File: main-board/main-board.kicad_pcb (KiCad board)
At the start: 2 copper layers, 210 x 130 mm, 199 parts, among them J1 PWR_SELECT, J10 Conn_02x05_Odd_Even, J11 Conn_02x05_Odd_Even, J12 Conn_02x05_Odd_Even, J13 Conn_02x05_Odd_Even, J14 Conn_02x05_Odd_Even, J15 Conn_02x05_Odd_Even, J16 COMM_3, J17 Modular board connector, J18 PWR_EXT_1, J19 PWR_EXT_2, J2 COMM1, J20 COMM_4, J21 COMM_OUT, J3 ICSP, J5 COMM_2, J7 Conn_02x05_Odd_Even, J8 Conn_02x05_Odd_Even, J9 Conn_02x05_Odd_Even, SW1 RESET, SW10 SW_Push, SW11 SW_Push, SW12 SW_SP3T_x08, SW13 SW_Push, SW14 SW_Push, SW15 SW_Push, SW16 SW_Push, SW17 SW_Push, SW18 SW_Push, SW19 SW_Push, SW2 BTN_LEVEL, SW20 SW_Push, SW21 SW_SP3T_x08, SW22 SW_Push, SW23 SW_Push, SW24 SW_Push, SW25 SW_Push, SW26 SW_Push, SW27 SW_Push, SW28 SW_Push, SW29 SW_Push, SW3 LED_GND, SW30 SW_SP3T_x08, SW31 SW_Push, SW32 SW_Push, SW33 SW_Push, SW34 SW_Push, SW35 SW_Push, SW36 SW_Push, SW37 SW_Push, SW38 SW_Push, SW39 SW_SP3T_x08, SW4 SW_Push, SW41 PWR_EN, SW5 SW_Push, SW6 SW_Push, SW7 SW_Push, SW8 SW_Push, SW9 SW_Push, U1 LM2576HVS-5, U2 AP1117-33, U3 AP1117-18, U4 FT232RL

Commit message: Changed ICP header to IDC connector
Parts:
- J3: footprint Connector_PinHeader_2.54mm:PinHeader_2x05_P2.54mm_Vertical -> Connector_IDC:IDC-Header_2x05_P2.54mm_Vertical
- TP_GND3: value VBUS -> GND
- TP_VBUS2: value GND -> VBUS
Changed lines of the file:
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@@
     (add_net "Net-(J17-Pad30)")
     (add_net "Net-(J17-Pad32)")
+    (add_net "Net-(J17-Pad34)")
+    (add_net "Net-(J17-Pad56)")
     (add_net "Net-(J17-Pad58)")
     (add_net "Net-(J17-Pad60)")
+    (add_net "Net-(J17-Pad75)")
     (add_net "Net-(J21-Pad2)")
     (add_net "Net-(J21-Pad3)")
@@
     (add_net "Net-(R71-Pad2)")
     (add_net "Net-(R72-Pad2)")
+    (add_net "Net-(SW41-Pad3)")
+    (add_net "Net-(U4-Pad10)")
+    (add_net "Net-(U4-Pad12)")
+    (add_net "Net-(U4-Pad13)")
+    (add_net "Net-(U4-Pad14)")
     (add_net "Net-(U4-Pad15)")
     (add_net "Net-(U4-Pad16)")
+    (add_net "Net-(U4-Pad19)")
+    (add_net "Net-(U4-Pad27)")
+    (add_net "Net-(U4-Pad28)")
+    (add_net "Net-(U4-Pad4)")
+    (add_net "Net-(U4-Pad6)")
+    (add_net "Net-(U4-Pad9)")
     (add_net VBUS)
   )
@@
     (uvia_drill 0.1)
   )
+  (module Connector_IDC:IDC-Header_2x05_P2.54mm_Vertical locked (layer F.Cu)
+    (at 66 140.8 270)
+    (descr "Through hole straight IDC box header, 2x05, 2.54mm pitch, double rows")
+    (tags "Through hole IDC box header THT 2x05 2.54mm double row")
+    (fp_text reference J3 (at 1.27 -6.604 90) (layer F.SilkS)
+      (effects (font (size 1 1) (thickness 0.15)))
+    )
+    (fp_text value ICSP (at 1.27 16.764 90) (layer F.Fab)
+      (effects (font (size 1 1) (thickness 0.15)))
+    )
+    (fp_line (start -3.655 -5.6) (end -1.115 -5.6) (layer F.SilkS) (width 0.12))
+    (fp_line (start -3.655 -5.6) (end -3.655 -3.06) (layer F.SilkS) (width 0.12))
+    (fp_line (start -3.405 -5.35) (end 5.945 -5.35) (layer F.SilkS) (width 0.12))
+    (fp_line (start -3.405 15.51) (end -3.405 -5.35) (layer F.SilkS) (width 0.12))
+    (fp_line (start 5.945 15.51) (end -3.405 15.51) (layer F.SilkS) (width 0.12))
+    (fp_line (start 5.945 -5.35) (end 5.945 15.51) (layer F.SilkS) (width 0.12))
+    (fp_line (start -3.41 -5.35) (end 5.95 -5.35) (layer F.CrtYd) (width 0.05))
+    (fp_line (start -3.41 15.51) (end -3.41 -5.35) (layer F.CrtYd) (width 0.05))
+    (fp_line (start 5.95 15.51) (end -3.41 15.51) (layer F.CrtYd) (width 0.05))
+    (fp_line (start 5.95 -5.35) (end 5.95 15.51) (layer F.CrtYd) (width 0.05))
+    (fp_line (start -3.155 15.26) (end -2.605 14.7) (layer F.Fab) (width 0.1))
+    (fp_line (start -3.155 -5.1) (end -2.605 -4.56) (layer F.Fab) (width 0.1))
+    (fp_line (start 5.695 15.26) (end 5.145 14.7) (layer F.Fab) (width 0.1))
+    (fp_line (start 5.695 -5.1) (end 5.145 -4.56) (layer F.Fab) (width 0.1))
+    (fp_line (start 5.145 14.7) (end -2.605 14.7) (layer F.Fab) (width 0.1))
+    (fp_line (start 5.695 15.26) (end -3.155 15.26) (layer F.Fab) (width 0.1))
+    (fp_line (start 5.145 -4.56) (end -2.605 -4.56) (layer F.Fab) (width 0.1))
+    (fp_line (start 5.695 -5.1) (end -3.155 -5.1) (layer F.Fab) (width 0.1))
+    (fp_line (start -2.605 7.33) (end -3.155 7.33) (layer F.Fab) (width 0.1))
+    (fp_line (start -2.605 2.83) (end -3.155 2.83) (layer F.Fab) (width 0.1))
+    (fp_line (start -2.605 7.33) (end -2.605 14.7) (layer F.Fab) (width 0.1))
+    (fp_line (start -2.605 -4.56) (end -2.605 2.83) (layer F.Fab) (width 0.1))
+    (fp_line (start -3.155 -5.1) (end -3.155 15.26) (layer F.Fab) (width 0.1))
+    (fp_line (start 5.145 -4.56) (end 5.145 14.7) (layer F.Fab) (width 0.1))
+    (fp_line (start 5.695 -5.1) (end 5.695 15.26) (layer F.Fab) (width 0.1))
+    (fp_text user %R (at 1.27 5.08 90) (layer F.Fab)
+      (effects (font (size 1 1) (thickness 0.15)))
+    )
+    (pad 10 thru_hole oval (at 2.54 10.16 270) (size 1.7272 1.7272) (drill 1.016) (layers *.Cu *.Mask)
+      (net 38 ICSP10))
+    (pad 9 thru_hole oval (at 0 10.16 270) (size 1.7272 1.7272) (drill 1.016) (layers *.Cu *.Mask)
+      (net 39 ICSP9))
+    (pad 8 thru_hole oval (at 2.54 7.62 270) (size 1.7272 1.7272) (drill 1.016) (layers *.Cu *.Mask)
+      (net 40 ICSP8))
+    (pad 7 thru_hole oval (at 0 7.62 270) (size 1.7272 1.7272) (drill 1.016) (layers *.Cu *.Mask)
+      (net 41 ICSP7))
+    (pad 6 thru_hole oval (at 2.54 5.08 270) (size 1.7272 1.7272) (drill 1.016) (layers *.Cu *.Mask)
+      (net 42 ICSP6))
+    (pad 5 thru_hole oval (at 0 5.08 270) (size 1.7272 1.7272) (drill 1.016) (layers *.Cu *.Mask)
+      (net 43 ICSP5))
+    (pad 4 thru_hole oval (at 2.54 2.54 270) (size 1.7272 1.7272) (drill 1.016) (layers *.Cu *.Mask)
+      (net 44 ICSP4))
+    (pad 3 thru_hole oval (at 0 2.54 270) (size 1.7272 1.7272) (drill 1.016) (layers *.Cu *.Mask)
+      (net 45 ICSP3))
+    (pad 2 thru_hole oval (at 2.54 0 270) (size 1.7272 1.7272) (drill 1.016) (layers *.Cu *.Mask)
+      (net 46 ICSP2))
+    (pad 1 thru_hole rect (at 0 0 270) (size 1.7272 1.7272) (drill 1.016) (layers *.Cu *.Mask)
+      (net 125 ICSP1))
+    (model ${KISYS3DMOD}/Connector_IDC.3dshapes/IDC-Header_2x05_P2.54mm_Vertical.wrl
+      (at (xyz 0 0 0))
+      (scale (xyz 1 1 1))
+      (rotate (xyz 0 0 0))
+    )
+  )
   (module TestPoint:TestPoint_Plated_Hole_D2.0mm (layer F.Cu)
     (at 162 144.9)
@@
     )
   )
-  (module Connector_PinHeader_2.54mm:PinHeader_2x05_P2.54mm_Vertical locked (layer F.Cu)
-    (at 66 140.8 270)
-    (descr "Through hole straight pin header, 2x05, 2.54mm pitch, double rows")
-    (tags "Through hole pin header THT 2x05 2.54mm double row")
-    (fp_text reference J3 (at 1.27 -2.33 90 unlocked) (layer F.SilkS) hide
-      (effects (font (size 0.7 0.7) (thickness 0.15)))
-    )
-    (fp_text value ICSP (at 1.27 12.49 90) (layer F.Fab)
-      (effects (font (size 1 1) (thickness 0.15)))
-    )
-    (fp_text user %R (at 1.27 5.08) (layer F.Fab) hide
-      (effects (font (size 1 1) (thickness 0.15)))
-    )
-    (fp_line (start 4.35 -1.8) (end -1.8 -1.8) (layer F.CrtYd) (width 0.05))
-    (fp_line (start 4.35 11.95) (end 4.35 -1.8) (layer F.CrtYd) (width 0.05))
-    (fp_line (start -1.8 11.95) (end 4.35 11.95) (layer F.CrtYd) (width 0.05))
-    (fp_line (start -1.8 -1.8) (end -1.8 11.95) (layer F.CrtYd) (width 0.05))
-    (fp_line (start -1.33 -1.33) (end 0 -1.33) (layer F.SilkS) (width 0.12))
-    (fp_line (start -1.33 0) (end -1.33 -1.33) (layer F.SilkS) (width 0.12))
-    (fp_line (start 1.27 -1.33) (end 3.87 -1.33) (layer F.SilkS) (width 0.12))
-    (fp_line (start 1.27 1.27) (end 1.27 -1.33) (layer F.SilkS) (width 0.12))
-    (fp_line (start -1.33 1.27) (end 1.27 1.27) (layer F.SilkS) (width 0.12))
-    (fp_line (start 3.87 -1.33) (end 3.87 11.49) (layer F.SilkS) (width 0.12))
-    (fp_line (start -1.33 1.27) (end -1.33 11.49) (layer F.SilkS) (width 0.12))
-    (fp_line (start -1.33 11.49) (end 3.87 11.49) (layer F.SilkS) (width 0.12))
-    (fp_line (start -1.27 0) (end 0 -1.27) (layer F.Fab) (width 0.1))
-    (fp_line (start -1.27 11.43) (end -1.27 0) (layer F.Fab) (width 0.1))
-    (fp_line (start 3.81 11.43) (end -1.27 11.43) (layer F.Fab) (width 0.1))
-    (fp_line (start 3.81 -1.27) (end 3.81 11.43) (layer F.Fab) (width 0.1))
-    (fp_line (start 0 -1.27) (end 3.81 -1.27) (layer F.Fab) (width 0.1))
-    (pad 10 thru_hole oval (at 2.54 10.16 270) (size 1.7 1.7) (drill 1) (layers *.Cu *.Mask)
-      (net 38 ICSP10))
-    (pad 9 thru_hole oval (at 0 10.16 270) (size 1.7 1.7) (drill 1) (layers *.Cu *.Mask)
-      (net 39 ICSP9))
-    (pad 8 thru_hole oval (at 2.54 7.62 270) (size 1.7 1.7) (drill 1) (layers *.Cu *.Mask)
-      (net 40 ICSP8))
-    (pad 7 thru_hole oval (at 0 7.62 270) (size 1.7 1.7) (drill 1) (layers *.Cu *.Mask)
-      (net 41 ICSP7))
-    (pad 6 thru_hole oval (at 2.54 5.08 270) (size 1.7 1.7) (drill 1) (layers *.Cu *.Mask)
-      (net 42 ICSP6))
-    (pad 5 thru_hole oval (at 0 5.08 270) (size 1.7 1.7) (drill 1) (layers *.Cu *.Mask)
-      (net 43 ICSP5))
-    (pad 4 thru_hole oval (at 2.54 2.54 270) (size 1.7 1.7) (drill 1) (layers *.Cu *.Mask)
-      (net 44 ICSP4))
-    (pad 3 thru_hole oval (at 0 2.54 270) (size 1.7 1.7) (drill 1) (layers *.Cu *.Mask)
-      (net 45 ICSP3))
-    (pad 2 thru_hole oval (at 2.54 0 270) (size 1.7 1.7) (drill 1) (layers *.Cu *.Mask)
-      (net 46 ICSP2))
-    (pad 1 thru_hole rect (at 0 0 270) (size 1.7 1.7) (drill 1) (layers *.Cu *.Mask)
-      (net 125 ICSP1))
-    (model ${KISYS3DMOD}/Connector_PinHeader_2.54mm.3dshapes/PinHeader_2x05_P2.54mm_Vertical.wrl
-      (at (xyz 0 0 0))
-      (scale (xyz 1 1 1))
-      (rotate (xyz 0 0 0))
-    )
-  )
   (module MountingHole:MountingHole_3.2mm_M3_ISO14580_Pad locked (layer F.Cu)
     (at 242 23)
@@
       (effects (font (size 1 1) (thickness 0.15)))
     )
-    (fp_text value VBUS (at 0 2.45) (layer F.Fab)
+    (fp_text value GND (at 0 2.45) (layer F.Fab)
       (effects (font (size 1 1) (thickness 0.15)))
     )
@@
       (effects (font (size 1 1) (thickness 0.15)))
     )
-    (fp_text value GND (at 0 2.45) (layer F.Fab)
+    (fp_text value VBUS (at 0 2.45) (layer F.Fab)
       (effects (font (size 1 1) (thickness 0.15)))
     )

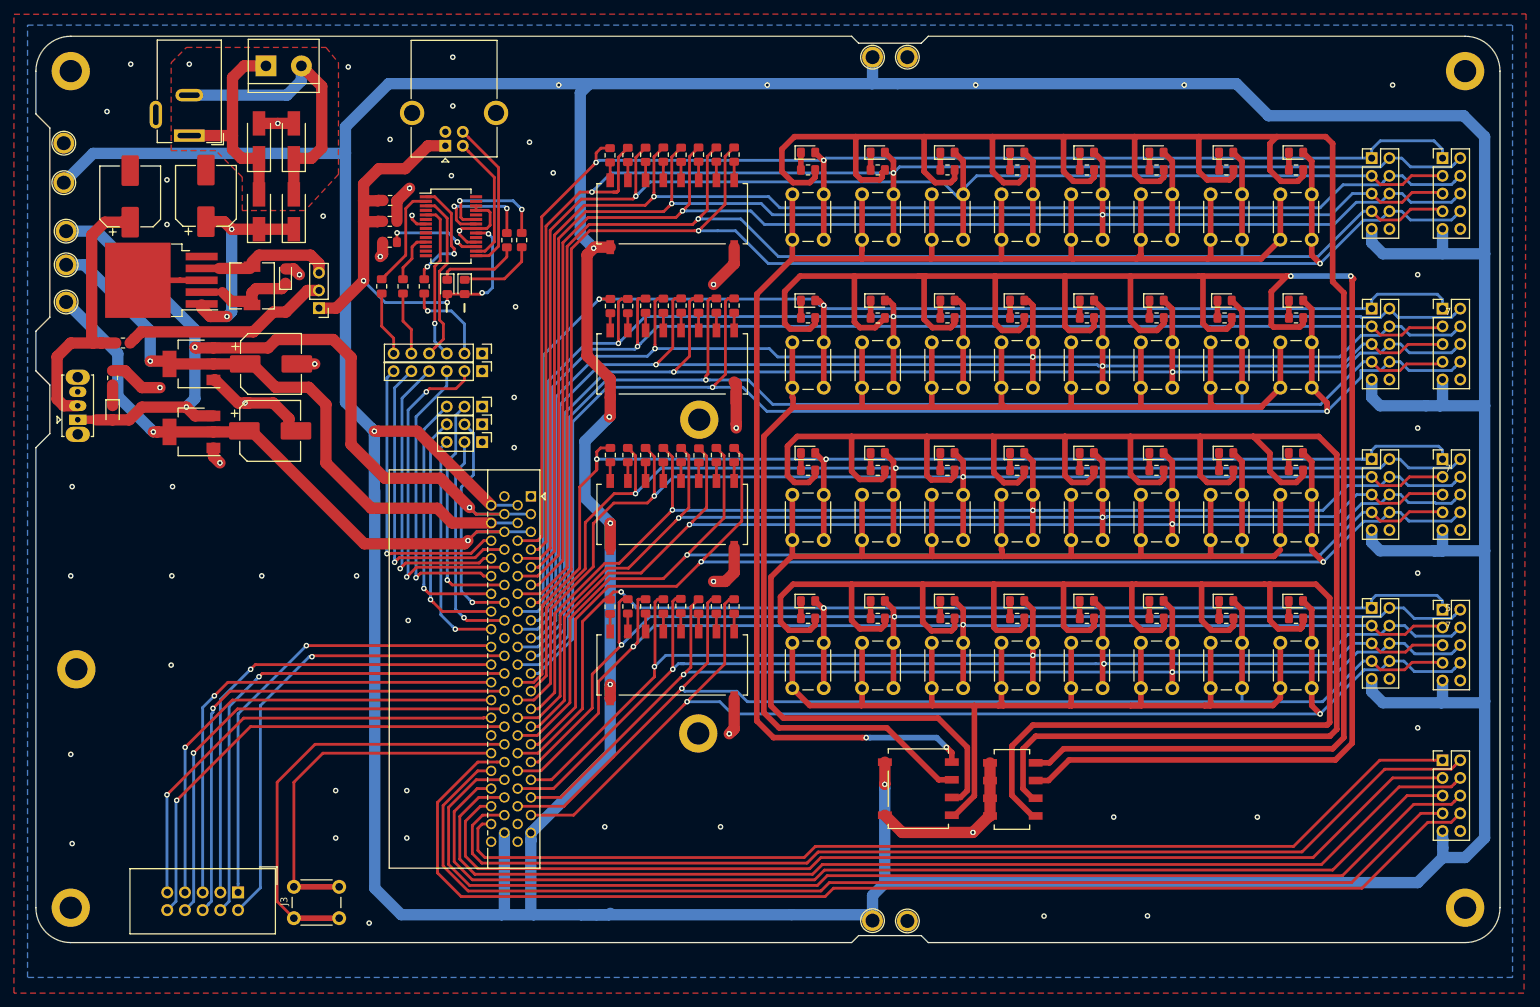
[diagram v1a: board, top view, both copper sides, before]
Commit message: Added silkscreen
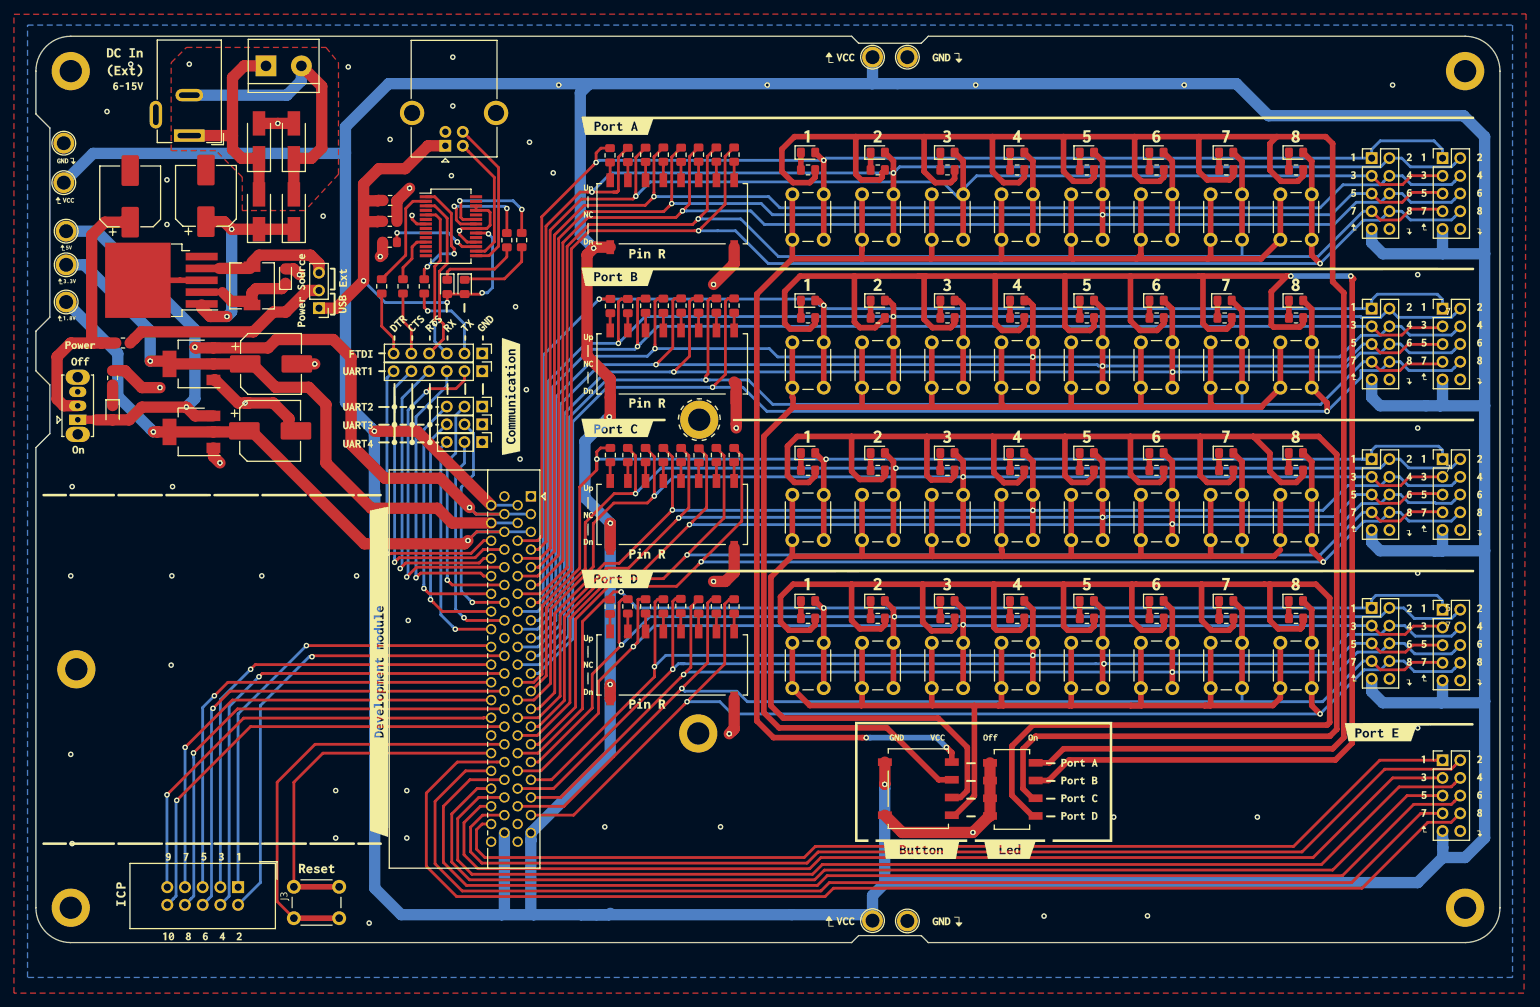
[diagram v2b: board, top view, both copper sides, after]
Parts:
- added ?: , , F.Cu at (131.8, 73.2)
- moved J3 0.75 mm to (66.0, 140.1)
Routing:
- net /PORT_E_PIN8: track 175.2 -> 178.6 mm
- net /PORT_E_PIN7: track 167.1 -> 169.6 mm
- net /PORT_E_PIN6: track 169.5 -> 170.9 mm
- net ICSP6: track 72.4 -> 71.6 mm
- net ICSP9: track 65.1 -> 64.3 mm
- net ICSP7: track 67.5 -> 66.8 mm
- net ICSP5: track 69.4 -> 68.6 mm
- net ICSP4: track 71.2 -> 70.4 mm
- net ICSP3: track 68.6 -> 67.8 mm
- net ICSP2: track 68.6 -> 67.9 mm
- net ICSP1: track 66.0 -> 65.3 mm
- net ICSP8: track 70.3 -> 69.6 mm
- net ICSP10: track 67.7 -> 67.1 mm
- net /PORT_E_PIN5: track 161.7 -> 162.2 mm

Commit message: Added final tweaks and logos
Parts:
- added Modular Development Board - Rev 1.1: LOGO_BRD_REF, qboards_aesthetics:logo_url-5mm, F.Cu at (195.0, 23.1)
- added [BRD_REF]: LOGO_BRD_REF, qboards_aesthetics:logo-20mm, F.Cu at (59.9, 108.7)
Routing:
- net VBUS: vias 10 -> 6
- net GND: vias 58 -> 60

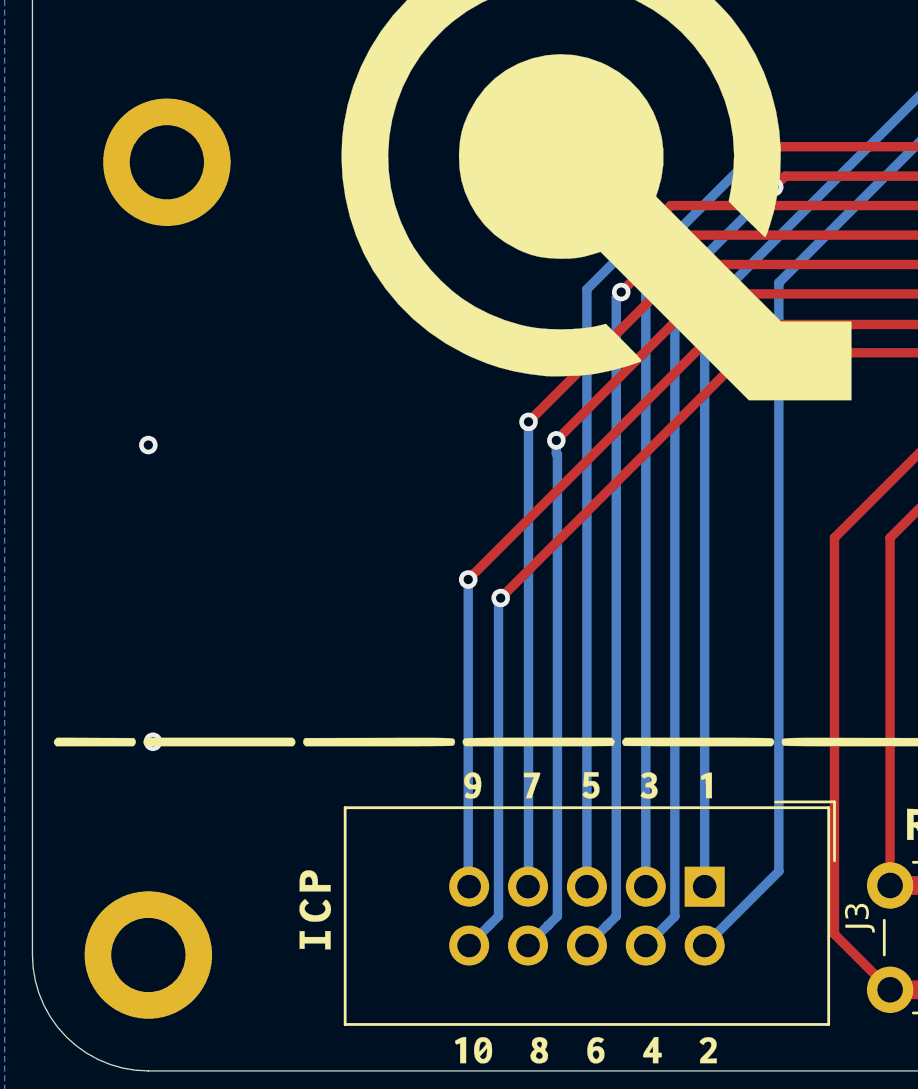
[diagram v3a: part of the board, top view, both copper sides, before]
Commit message: Fixed DRC errors
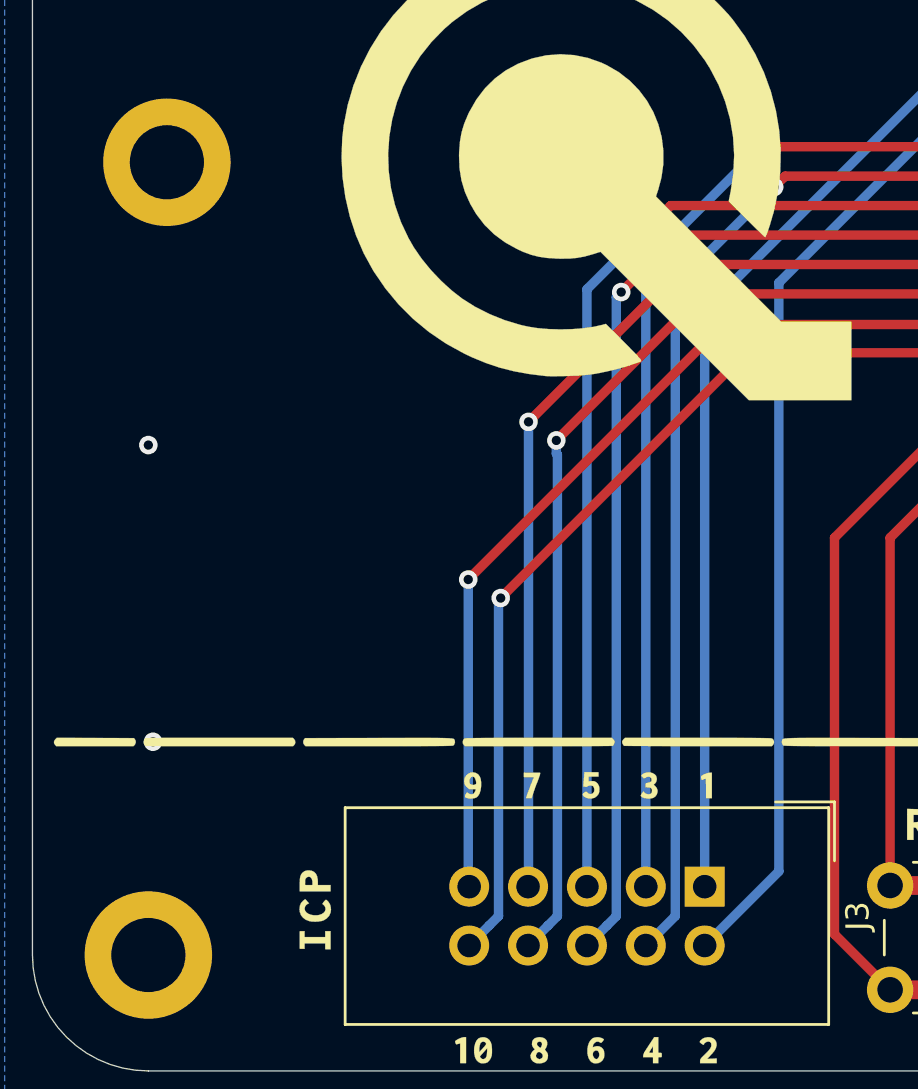
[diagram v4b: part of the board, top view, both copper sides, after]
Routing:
- net GND: vias 60 -> 59
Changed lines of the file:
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@@
     (thickness 1.6)
     (drawings 38)
-    (tracks 2112)
+    (tracks 2111)
     (zones 0)
     (modules 202)
@@
     (33 F.Adhes user hide)
     (34 B.Paste user hide)
-    (35 F.Paste user hide)
-    (36 B.SilkS user)
+    (35 F.Paste user)
+    (36 B.SilkS user hide)
     (37 F.SilkS user)
     (38 B.Mask user hide)
-    (39 F.Mask user hide)
+    (39 F.Mask user)
     (40 Dwgs.User user hide)
     (41 Cmts.User user hide)
@@
     (45 Margin user hide)
     (46 B.CrtYd user hide)
-    (47 F.CrtYd user hide)
+    (47 F.CrtYd user)
     (48 B.Fab user hide)
     (49 F.Fab user)
@@
       (drillshape 0)
       (scaleselection 1)
-      (outputdirectory "../../../Desktop/pcb/gerbers/"))
+      (outputdirectory "C:/Users/Wilco/Desktop/pcb/gerbers/"))
   )
   (net 0 "")
@@
   (via (at 56.5 95.4) (size 0.8) (drill 0.4) (layers F.Cu B.Cu) (net 1))
   (via (at 42 95.4) (size 0.8) (drill 0.4) (layers F.Cu B.Cu) (net 1))
-  (via (at 42 108.2) (size 0.8) (drill 0.4) (layers F.Cu B.Cu) (net 1))
   (via (at 42 121) (size 0.8) (drill 0.4) (layers F.Cu B.Cu) (net 1))
   (via (at 42.2 133.8) (size 0.8) (drill 0.4) (layers F.Cu B.Cu) (net 1))
@@
   (via (at 69 109.86679) (size 0.8) (drill 0.4) (layers F.Cu B.Cu) (net 44))
   (segment (start 104.2 109.4) (end 69.46679 109.4) (width 0.4064) (layer F.Cu) (net 44))
-  (segment (start 64.713201 141.336799) (end 63.46 142.59) (width 0.4064) (layer B.Cu) (net 44))
-  (segment (start 69 109.86679) (end 64.713201 114.153589) (width 0.4064) (layer B.Cu) (net 44))
-  (segment (start 64.713201 114.153589) (end 64.713201 141.336799) (width 0.4064) (layer B.Cu) (net 44))
+  (segment (start 64.7319 141.3181) (end 63.46 142.59) (width 0.4064) (layer B.Cu) (net 44))
+  (segment (start 69 109.86679) (end 64.7319 114.13489) (width 0.4064) (layer B.Cu) (net 44))
+  (segment (start 64.7319 114.13489) (end 64.7319 141.3181) (width 0.4064) (layer B.Cu) (net 44))
   (via (at 67.8 108.8) (size 0.8) (drill 0.4) (layers F.Cu B.Cu) (net 45))
   (segment (start 102.3 108.13) (end 68.47 108.13) (width 0.4064) (layer F.Cu) (net 45))
